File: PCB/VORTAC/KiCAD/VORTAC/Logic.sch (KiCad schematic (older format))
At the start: 8 parts

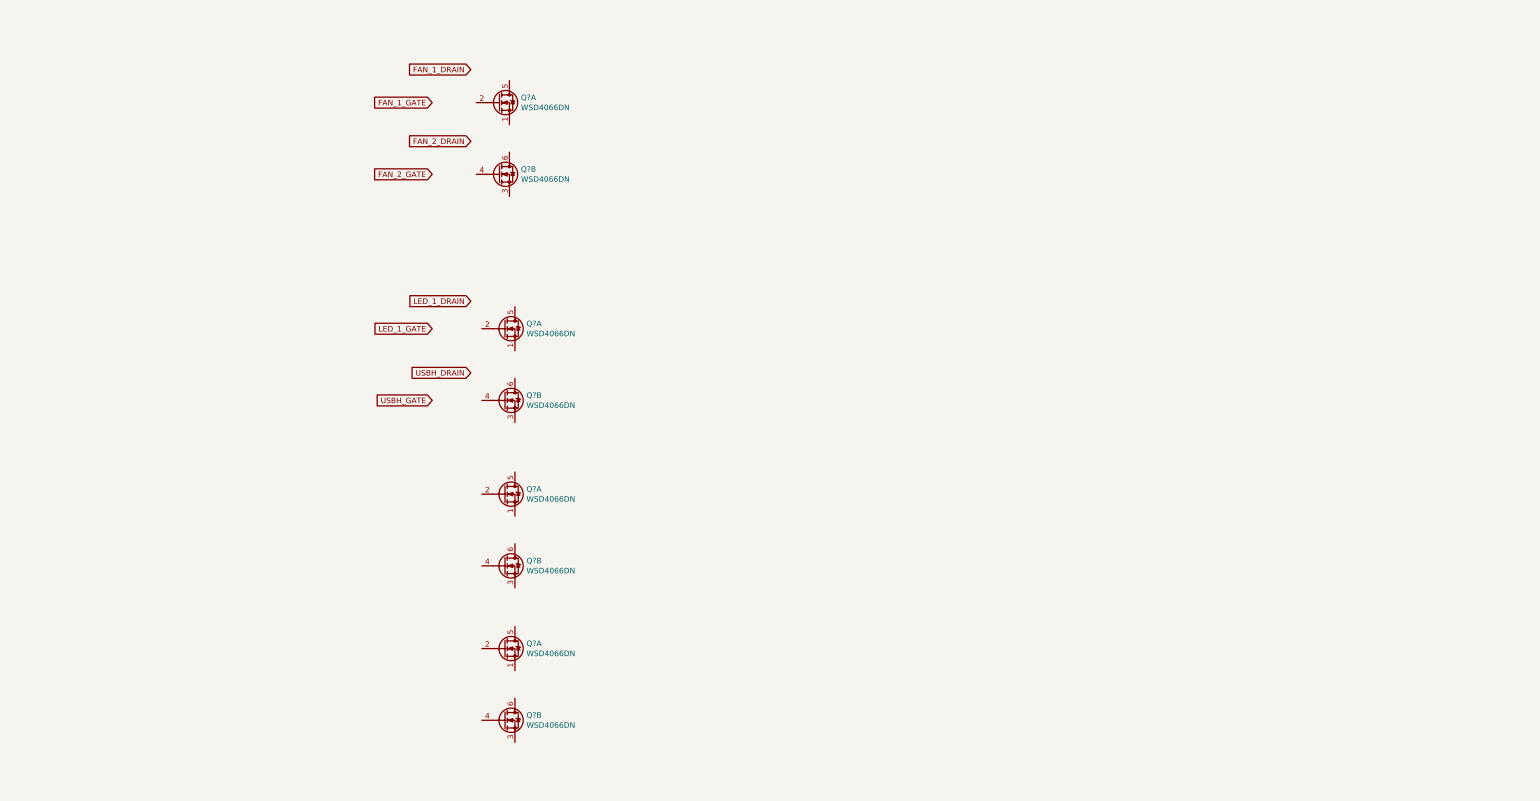
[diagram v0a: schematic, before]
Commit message: updated schematics
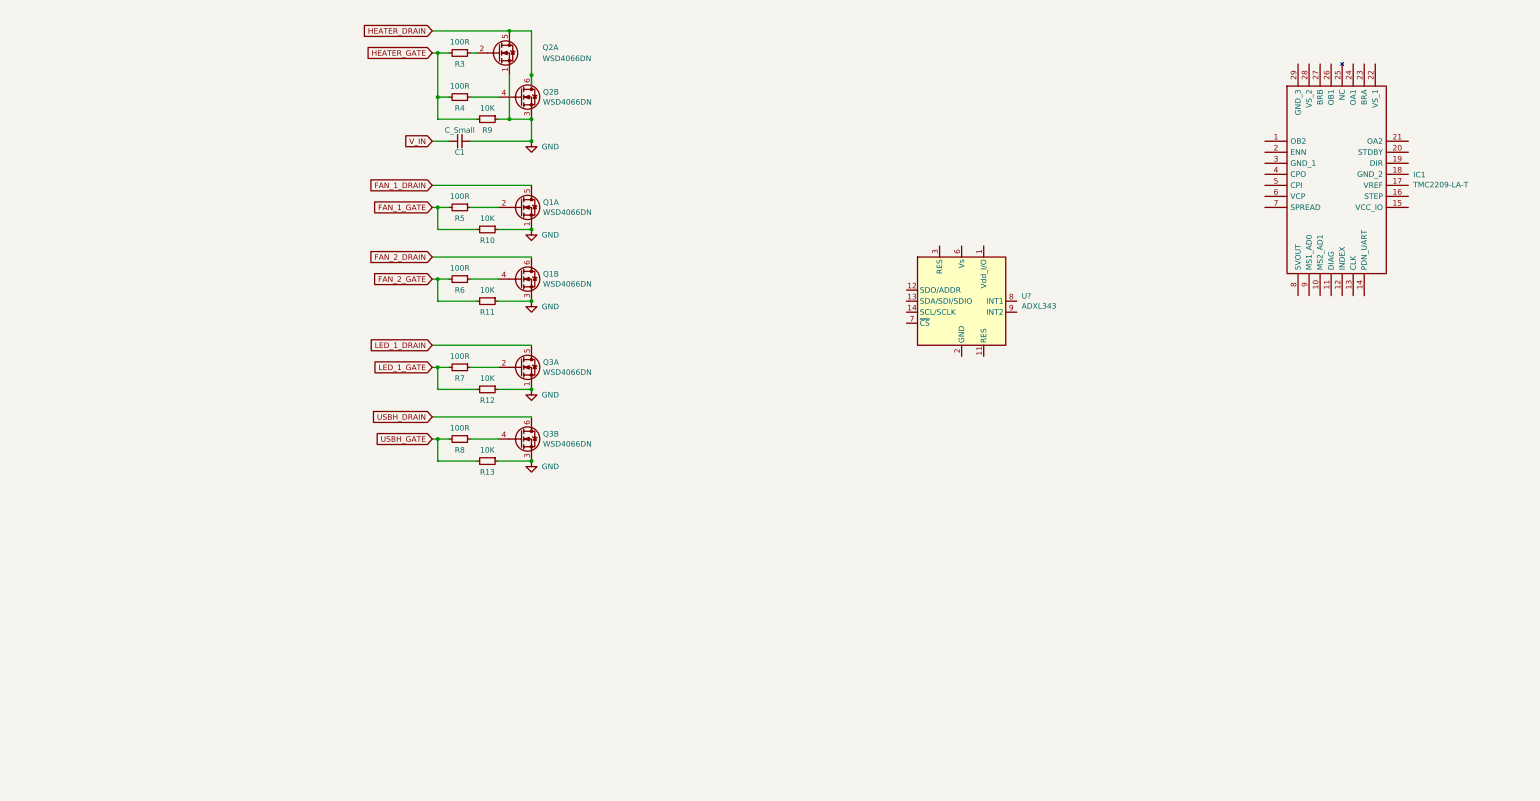
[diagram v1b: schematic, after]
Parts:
- removed Q? (x6): WSD4066DN, symbol ToolChanger:WSD4066DN
- added C1: C_Small, symbol Device:C_Small
- added IC1: TMC2209-LA-T, ToolChanger:tmc_2209_package, symbol ToolChanger:TMC2209-LA-T
- added Q2, Q3: WSD4066DN, ToolChanger:WSD4066DN, symbol ToolChanger:WSD4066DN
- added R10, R11, R12, R13, R9: 10K, Resistor_SMD:R_0402_1005Metric, symbol Device:R_Small
- added R3, R4, R5, R6, R7, R8: 100R, Resistor_SMD:R_0402_1005Metric, symbol Device:R_Small
- added U?: ADXL343, Package_LGA:LGA-14_3x5mm_P0.8mm_LayoutBorder1x6y, symbol Sensor_Motion:ADXL343
- Q1: renamed from Q?; footprint (none) -> ToolChanger:WSD4066DN
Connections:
- net FAN_1_DRAIN: now also Q1.5 (D2)
- net FAN_1_GATE: now also R10.2, R5.2
- net FAN_2_DRAIN: now also Q1.6 (D2)
- net FAN_2_GATE: now also R11.2, R6.2
- net LED_1_DRAIN: now also Q3.5 (D2)
- net LED_1_GATE: now also R12.2, R7.2
- net USBH_DRAIN: now also Q3.6 (D2)
- net USBH_GATE: now also R13.2, R8.2
- net GND: now reaches Q1.1 (S2)
- net GND: now also Q1.3 (S2), C1.2, Q2.1 (S2), Q2.3 (S2), Q3.1 (S2), Q3.3 (S2), R10.1, R11.1, R12.1, R13.1, R9.1
- net at Q1.2 (G2): now also R5.1
- net at Q1.4 (G2): now also R6.1
- new net: Q2.4 (G2), R4.1
- new net: Q2.2 (G2), R3.1
- new net: Q3.4 (G2), R8.1
- new net: Q3.2 (G2), R7.1
- new net: U?.2 (GND), U?.4 (GND), U?.5 (GND)
- new net HEATER_DRAIN: Q2.5 (D2), Q2.6 (D2)
- new net HEATER_GATE: R3.2, R4.2, R9.2
- new net V_IN: C1.1
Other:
- moved on the sheet: Q1A, Q1B

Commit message: TMC and Acc preperation
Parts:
- added C?: C_Small, symbol Device:C_Small
- added C?: 22n/50V, symbol Device:C_Small
- added C?: 100n/16V, symbol Device:C_Small
- added C?: 2.2μ/6.3V, symbol Device:C_Small
- added C? (x2): 100nV, symbol Device:C_Small
- added C?: 100uF/35V, symbol Device:CP
- added C?: 100n, symbol Device:C_Small
- added R? (x2): 22k, symbol Device:R_Small
- added R?: 22K, symbol Device:R_Small
- added R?: 1K, symbol Device:R_Small
- added R? (x2): ???, symbol Device:R_Small
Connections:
- net GND: now also IC1.10 (MS2_AD1), IC1.18 (GND_2), IC1.20 (STDBY), IC1.29 (GND_3), IC1.3 (GND_1), IC1.7 (SPREAD), IC1.9 (MS1_AD0), U?.2 (GND), U?.4 (GND), U?.5 (GND), C?.1, C?.1, C?.2, C?.2, C?.2, C?.2, R?.1, R?.1, R?.2, R?.2
- net STEP_1_B2: now reaches IC1.1 (OB2)
- net TMC_DIAG: now reaches IC1.11 (DIAG)
- net at IC1.13 (CLK): now also R?.1
- net TMC_UART_RX: now reaches IC1.14 (PDN_UART)
- net TMC_UART_RX: now also R?.1, R?.1
- net 3.3V: now reaches IC1.15 (VCC_IO)
- net 3.3V: now also U?.1 (Vdd_I/O), C?.1, C?.1, R?.1
- net TMC_STEP: now reaches IC1.16 (STEP)
- net TMC_DIR: now reaches IC1.19 (DIR)
- net TMC_ENN: now reaches IC1.2 (ENN)
- net TMC_ENN: now also R?.2
- net STEP_1_A2: now reaches IC1.21 (OA2)
- net TMC_VS: now reaches IC1.22 (VS_1)
- net TMC_VS: now also IC1.28 (VS_2), C?.1, C?.2, C?.2, C?.2
- net TMC_BRA: now reaches IC1.23 (BRA)
- net TMC_BRA: now also R?.2
- net STEP_1_A1: now reaches IC1.24 (OA1)
- net STEP_1_B1: now reaches IC1.26 (OB1)
- net TMC_BRB: now reaches IC1.27 (BRB)
- net TMC_BRB: now also R?.2
- net at IC1.4 (CPO): now also C?.2
- net at IC1.5 (CPI): now also C?.1
- net at IC1.6 (VCP): now also C?.1
- net at IC1.8 (5VOUT): now also C?.1
- net ADXL_SDO: now reaches U?.12 (SDO/ADDR)
- net ADXL_SDI: now reaches U?.13 (SDA/SDI/SDIO)
- net ADXL_SCL: now reaches U?.14 (SCL/SCLK)
- net ADXL_AREF: now reaches U?.6 (Vs)
- net ADXL_CS: now reaches U?.7 (~CS)
- net ADXL_INT1: now reaches U?.8 (INT1)
- new net TMC_UART_TX: R?.2
- no-connect marks 0 -> 5
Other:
- moved on the sheet: IC1, U?

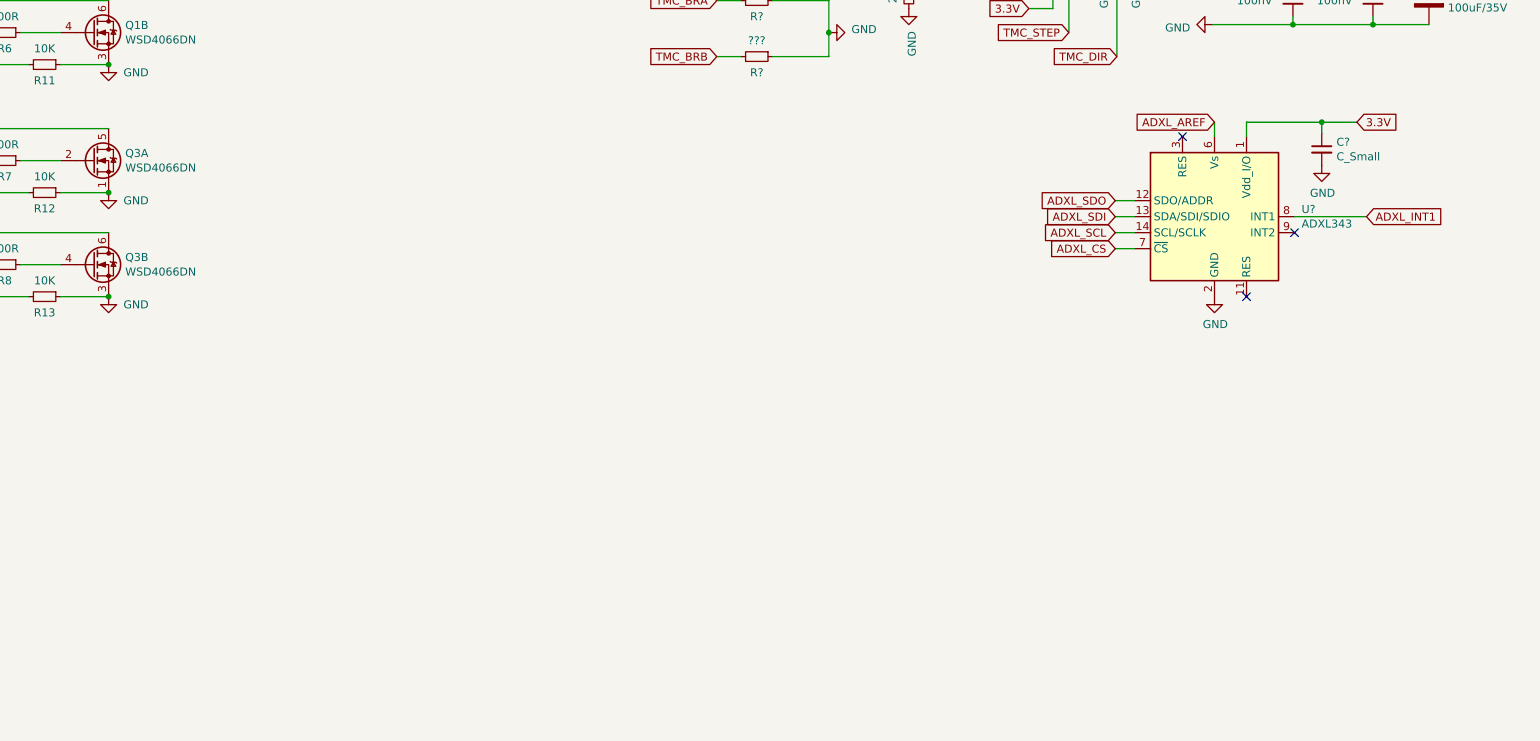
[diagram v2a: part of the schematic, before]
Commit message: GitIgnore and Footprints
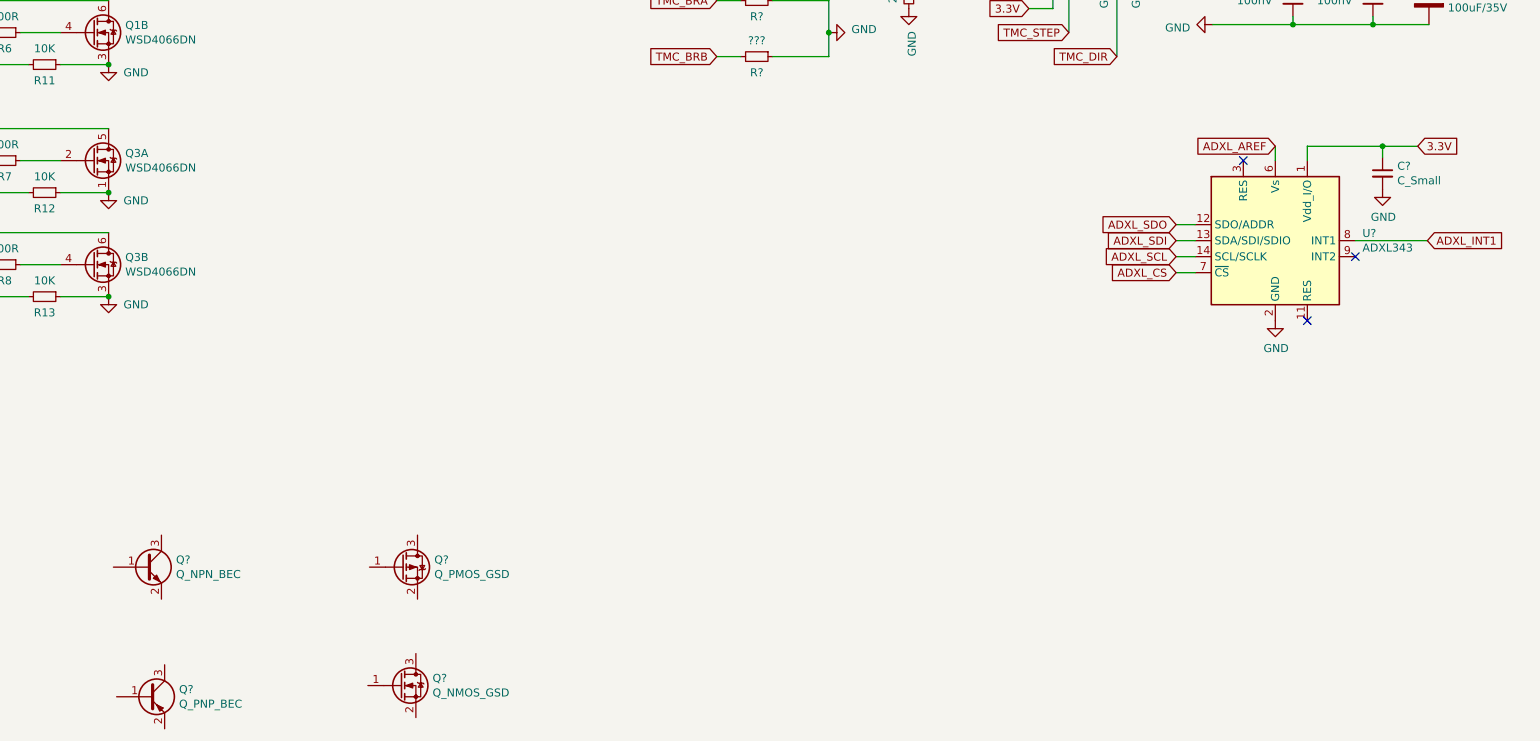
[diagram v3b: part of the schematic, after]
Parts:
- added Q?: Q_NPN_BEC, Package_TO_SOT_SMD:SOT-23, symbol Device:Q_NPN_BEC
- added Q?: Q_PNP_BEC, Package_TO_SOT_SMD:SOT-23, symbol Device:Q_PNP_BEC
- added Q?: Q_PMOS_GSD, ToolChanger:IRF9310PbF-1_SO-8, symbol Device:Q_PMOS_GSD
- added Q?: Q_NMOS_GSD, ToolChanger:IRF9310PbF-1_SO-8, symbol Device:Q_NMOS_GSD
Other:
- moved on the sheet: C?, U?
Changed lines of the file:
@@
 L Sensor_Motion:ADXL343 U?
 U 1 1 6157ACF9
-P 9060 4150
-F 0 "U?" H 9604 4196 50  0000 L CNN
-F 1 "ADXL343" H 9604 4105 50  0000 L CNN
-F 2 "Package_LGA:LGA-14_3x5mm_P0.8mm_LayoutBorder1x6y" H 9060 4150 50  0001 C CNN
-F 3 "https://www.analog.com/media/en/technical-documentation/data-sheets/ADXL343.pdf" H 9060 4150 50  0001 C CNN
-	1    9060 4150
-	1    0    0    -1
-$EndComp
-Text GLabel 9950 3560 2    50   Input ~ 0
+P 9440 4300
+F 0 "U?" H 9984 4346 50  0000 L CNN
+F 1 "ADXL343" H 9984 4255 50  0000 L CNN
+F 2 "Package_LGA:LGA-14_3x5mm_P0.8mm_LayoutBorder1x6y" H 9440 4300 50  0001 C CNN
+F 3 "https://www.analog.com/media/en/technical-documentation/data-sheets/ADXL343.pdf" H 9440 4300 50  0001 C CNN
+	1    9440 4300
+	1    0    0    -1
+$EndComp
+Text GLabel 10330 3710 2    50   Input ~ 0
 3.3V
 $Comp
 L power:GND #PWR?
 U 1 1 614DF03A
-P 9730 3830
-F 0 "#PWR?" H 9730 3580 50  0001 C CNN
-F 1 "GND" H 9735 3657 50  0000 C CNN
-F 2 "" H 9730 3830 50  0001 C CNN
-F 3 "" H 9730 3830 50  0001 C CNN
-	1    9730 3830
+P 10110 3980
+F 0 "#PWR?" H 10110 3730 50  0001 C CNN
+F 1 "GND" H 10115 3807 50  0000 C CNN
+F 2 "" H 10110 3980 50  0001 C CNN
+F 3 "" H 10110 3980 50  0001 C CNN
+	1    10110 3980
 	1    0    0    -1
 $EndComp
@@
 L Device:C_Small C?
 U 1 1 614E163D
-P 9730 3730
-F 0 "C?" H 9822 3776 50  0000 L CNN
-F 1 "C_Small" H 9822 3685 50  0000 L CNN
-F 2 "" H 9730 3730 50  0001 C CNN
-F 3 "~" H 9730 3730 50  0001 C CNN
-	1    9730 3730
-	1    0    0    -1
-$EndComp
-Wire Wire Line
-	9260 3650 9260 3560
-Wire Wire Line
-	9260 3560 9730 3560
-Wire Wire Line
-	9730 3630 9730 3560
-Connection ~ 9730 3560
-Wire Wire Line
-	9730 3560 9950 3560
-Text GLabel 10010 4150 2    50   Input ~ 0
+P 10110 3880
+F 0 "C?" H 10202 3926 50  0000 L CNN
+F 1 "C_Small" H 10202 3835 50  0000 L CNN
+F 2 "" H 10110 3880 50  0001 C CNN
+F 3 "~" H 10110 3880 50  0001 C CNN
+	1    10110 3880
+	1    0    0    -1
+$EndComp
+Wire Wire Line
+	9640 3800 9640 3710
+Wire Wire Line
+	9640 3710 10110 3710
+Wire Wire Line
+	10110 3780 10110 3710
+Connection ~ 10110 3710
+Wire Wire Line
+	10110 3710 10330 3710
+Text GLabel 10390 4300 2    50   Input ~ 0
 ADXL_INT1
 Wire Wire Line
-	9560 4150 10010 4150
+	9940 4300 10390 4300
 $Comp
 L power:GND #PWR?
 U 1 1 614F0BEC
-P 9060 4650
-F 0 "#PWR?" H 9060 4400 50  0001 C CNN
-F 1 "GND" H 9065 4477 50  0000 C CNN
-F 2 "" H 9060 4650 50  0001 C CNN
-F 3 "" H 9060 4650 50  0001 C CNN
-	1    9060 4650
-	1    0    0    -1
-$EndComp
-Text GLabel 8440 4350 0    50   Input ~ 0
+P 9440 4800
+F 0 "#PWR?" H 9440 4550 50  0001 C CNN
+F 1 "GND" H 9445 4627 50  0000 C CNN
+F 2 "" H 9440 4800 50  0001 C CNN
+F 3 "" H 9440 4800 50  0001 C CNN
+	1    9440 4800
+	1    0    0    -1
+$EndComp
+Text GLabel 8820 4500 0    50   Input ~ 0
 ADXL_CS
-Text GLabel 8440 4250 0    50   Input ~ 0
+Text GLabel 8820 4400 0    50   Input ~ 0
 ADXL_SCL
-Text GLabel 8440 4150 0    50   Input ~ 0
+Text GLabel 8820 4300 0    50   Input ~ 0
 ADXL_SDI
-Text GLabel 8440 4050 0    50   Input ~ 0
+Text GLabel 8820 4200 0    50   Input ~ 0
 ADXL_SDO
 Wire Wire Line
-	8440 4050 8560 4050
-Wire Wire Line
-	8560 4150 8440 4150
-Wire Wire Line
-	8440 4250 8560 4250
-Wire Wire Line
-	8560 4350 8440 4350
-Text GLabel 9060 3560 0    50   Input ~ 0
+	8820 4200 8940 4200
+Wire Wire Line
+	8940 4300 8820 4300
+Wire Wire Line
+	8820 4400 8940 4400
+Wire Wire Line
+	8940 4500 8820 4500
+Text GLabel 9440 3710 0    50   Input ~ 0
 ADXL_AREF
 Wire Wire Line
-	9060 3650 9060 3560
-NoConn ~ 9260 4650
-NoConn ~ 8860 3650
-NoConn ~ 9560 4250
+	9440 3800 9440 3710
+NoConn ~ 9640 4800
+NoConn ~ 9240 3800
+NoConn ~ 9940 4400
 Text GLabel 10450 1900 2    50   Input ~ 0
 STEP_1_A1
@@
 Wire Wire Line
 	6100 2800 5950 2800
+$Comp
+L Device:Q_NPN_BEC Q?
+U 1 1 61599DC1
+P 2380 6340
+F 0 "Q?" H 2571 6386 50  0000 L CNN
+F 1 "Q_NPN_BEC" H 2571 6295 50  0000 L CNN
+F 2 "Package_TO_SOT_SMD:SOT-23" H 2580 6440 50  0001 C CNN
+F 3 "https://lcsc.com/product-detail/Bipolar-Transistors-BJT_Changjiang-Electronics-Tech-CJ-SS8050_C2150.html" H 2380 6340 50  0001 C CNN
+F 4 "C2150" H 2380 6340 50  0001 C CNN "LCSC"
+	1    2380 6340
+	1    0    0    -1
+$EndComp
+$Comp
+L Device:Q_PNP_BEC Q?
+U 1 1 615A2596
+P 2400 7150
+F 0 "Q?" H 2590 7196 50  0000 L CNN
+F 1 "Q_PNP_BEC" H 2590 7105 50  0000 L CNN
+F 2 "Package_TO_SOT_SMD:SOT-23" H 2600 7250 50  0001 C CNN
+F 3 "https://lcsc.com/product-detail/Bipolar-Transistors-BJT_Changjiang-Electronics-Tech-CJ-SS8550-Y2_C8542.html" H 2400 7150 50  0001 C CNN
+F 4 "C8542" H 2400 7150 50  0001 C CNN "LCSC"
+	1    2400 7150
+	1    0    0    -1
+$EndComp
+$Comp
+L Device:Q_PMOS_GSD Q?
+U 1 1 615B049F
+P 3980 6340
+F 0 "Q?" H 4185 6386 50  0000 L CNN
+F 1 "Q_PMOS_GSD" H 4185 6295 50  0000 L CNN
+F 2 "ToolChanger:IRF9310PbF-1_SO-8" H 4180 6440 50  0001 C CNN
+F 3 "https://datasheet.lcsc.com/lcsc/1811141221_Infineon-Technologies-IRF9310TRPBF_C92305.pdf" H 3980 6340 50  0001 C CNN
+F 4 "C92305" H 3980 6340 50  0001 C CNN "LCSC"
+	1    3980 6340
+	1    0    0    -1
+$EndComp
+$Comp
+L Device:Q_NMOS_GSD Q?
+U 1 1 615B6960
+P 3970 7080
+F 0 "Q?" H 4174 7126 50  0000 L CNN
+F 1 "Q_NMOS_GSD" H 4174 7035 50  0000 L CNN
+F 2 "ToolChanger:IRF9310PbF-1_SO-8" H 4170 7180 50  0001 C CNN
+F 3 "https://datasheet.lcsc.com/lcsc/1809192221_Infineon-Technologies-IRF8736TRPBF_C51630.pdf" H 3970 7080 50  0001 C CNN
+F 4 "C51630" H 3970 7080 50  0001 C CNN "LCSC"
+	1    3970 7080
+	1    0    0    -1
+$EndComp
 $EndSCHEMATC

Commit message: Schematic and Lib Updates
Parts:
- removed Q?: Q_PMOS_GSD, ToolChanger:IRF9310PbF-1_SO-8, symbol Device:Q_PMOS_GSD
- added C2: C_Small, symbol Device:C_Small
- added D1, D2, D3, D4: D, Diode_SMD:D_SOD-123F, symbol Device:D
- added Q4: Q_NMOS_GSD, ToolChanger:IRF9310PbF-1_SO-8, symbol Device:Q_NMOS_GSD
- added Q8: Q_PMOS_GSD, ToolChanger:IRF9310PbF-1_SO-8, symbol Device:Q_PMOS_GSD
- added R14: 100R, Resistor_SMD:R_0402_1005Metric, symbol Device:R_Small
- added R15: 10K, Resistor_SMD:R_0402_1005Metric, symbol Device:R_Small
- added R22, R23, R24, R25, R26, R27: 220K, Resistor_SMD:R_0402_1005Metric, symbol Device:R_Small
- gave numbers to parts that had none: 18
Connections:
- net GND: now also Q7.2 (S), C2.2, Q4.2 (S), R15.1, R23.2
- net HEATER_DRAIN: now also Q4.3 (D)
- net HEATER_GATE: now also R14.2, R15.2
- net V_IN: now also C2.1, Q8.2 (S), R22.1
- net at Q5.1 (B): now also D4.1 (K), R27.2
- net at Q5.2 (E): now also R26.1
- net at Q5.3 (C): now also D1.1 (K), Q8.1 (G)
- net at Q6.1 (B): now also D3.2 (A), R25.1
- net at Q6.2 (E): now also R24.2
- net at Q6.3 (C): now also Q7.1 (G), D2.2 (A)
- net DOCK_GND: now reaches Q7.3 (D)
- net DOCK_GND: now also D4.2 (A), R25.2, R26.2
- new net: D1.2 (A), R22.2
- new net: D2.1 (K), R23.1
- new net: Q4.1 (G), R14.1
- new net DOCK_V_IN: D3.1 (K), Q8.3 (D), R24.1, R27.1
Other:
- note added: "ADXL_345"
- note added: "FAN MOSFET - WSD4066DN"
- note added: "HEATER MOSFET - Infineon Technologies IRF8736TRPBF"
- note added: "LED/USB MOSFET - WSD4066DN"
- note added: "Reverse Voltage & Reverse Grabber Leakage Protection"
- note added: "TMC2209"
- note added: "TODO: This needs to be changed to ADXL345"
- note added: "TODO: add output protection"
- note added: "to be deleted"
- moved on the sheet: C1, C10, C3, C4, C5, C6, C7, C8, C9, IC1, Q1A, Q1B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

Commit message: pushie
updates and stuff
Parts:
- removed Q2: WSD4066DN, ToolChanger:WSD4066DN, symbol ToolChanger:WSD4066DN
- removed R3, R4: 100R, Resistor_SMD:R_0402_1005Metric, symbol Device:R_Small
- C1: value C_Small -> 0.1uF; footprint (none) -> Capacitor_SMD:C_0402_1005Metric_Pad0.74x0.62mm_HandSolder
- D1, D2, D3, D4: footprint Diode_SMD:D_SOD-123F -> Diode_SMD:D_SOD-923
- R22, R23, R24, R25, R26, R27: value 220K -> 100K
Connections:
- net GND: no longer R9.1
- net HEATER_GATE: no longer R9.2
- net V_IN: no longer C1.1
- net TMC_BRA: no longer names the net of IC1.23 (BRA)
- net TMC_BRA: now also R17.2; no longer R16.2
- net TMC_BRB: no longer names the net of IC1.27 (BRB)
- net TMC_BRB: now also R16.2; no longer R17.2
- new net THERM_1: C1.1, R9.1
- new net THERM_1_PIN: R9.2
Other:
- note added: "consider changing to AGND"
- note added: "consider changing to WSD4066DN"
- note removed: "to be deleted"
- moved on the sheet: R16, R17
